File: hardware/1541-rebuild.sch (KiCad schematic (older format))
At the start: 9 parts, among them IC1 ATMEGA1284P-P, SW1 SW_PUSH, SW2 SW_PUSH, SW3 SW_PUSH, X1 20Mhz

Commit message: WPS Signal zum Diskwechsel anzeigen eingebaut. Laden des Track18 eines ausgewählten G64. Schaltpaln aktuallisiert
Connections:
- wire segments 82 -> 85
- no-connect marks 6 -> 5
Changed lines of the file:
@@
 F7 "EN" I B 6950 1900 60
 $EndSheet
-NoConn ~ 6100 4300
 NoConn ~ 6100 4400
 NoConn ~ 6100 4600
@@
 F15 "SOE" I L 6600 4500 60
 F16 "MTR" I R 7700 4300 60
+F17 "WPS" I L 6600 4600 60
 $EndSheet
-Wire Wire Line
-	3400 2900 4100 2900
-Wire Wire Line
-	1800 2900 2000 2900
-Connection ~ 1900 2900
-Wire Wire Line
-	1800 3200 2000 3200
-Connection ~ 1900 3200
-Wire Wire Line
-	4900 5800 4900 5900
-Wire Wire Line
-	4900 5900 5100 5900
-Wire Wire Line
-	5000 5900 5000 5950
-Wire Wire Line
-	5100 5900 5100 5800
-Connection ~ 5000 5900
-Wire Wire Line
-	4900 1800 4900 1700
-Wire Wire Line
-	4900 1700 5100 1700
-Wire Wire Line
-	5000 1700 5000 1650
-Wire Wire Line
-	5100 1700 5100 1800
-Connection ~ 5000 1700
-Wire Wire Line
-	3700 2100 3600 2100
-Wire Wire Line
-	4000 2100 4100 2100
-Wire Wire Line
-	1200 1050 1200 1550
-Connection ~ 1200 1250
-Wire Wire Line
-	1500 1050 1500 1550
-Connection ~ 1500 1250
-Wire Wire Line
-	6450 1900 6450 2100
-Wire Wire Line
-	6450 2100 6100 2100
-Wire Wire Line
-	6550 1900 6550 2200
-Wire Wire Line
-	6550 2200 6100 2200
-Wire Wire Line
-	6650 1900 6650 2300
-Wire Wire Line
-	6650 2300 6100 2300
-Wire Wire Line
-	6750 1900 6750 2400
-Wire Wire Line
-	6750 2400 6100 2400
-Wire Wire Line
-	6850 1900 6850 2500
-Wire Wire Line
-	6850 2500 6100 2500
-Wire Wire Line
-	6950 1900 6950 2600
-Wire Wire Line
-	6950 2600 6100 2600
-Wire Wire Line
-	6100 4800 6600 4800
-Wire Wire Line
-	6100 4900 6600 4900
-Wire Wire Line
-	6100 5000 6600 5000
-Wire Wire Line
-	6100 5100 6600 5100
-Wire Wire Line
-	6100 5200 6600 5200
-Wire Wire Line
-	6100 5300 6600 5300
-Wire Wire Line
-	6100 5400 6600 5400
-Wire Wire Line
-	6100 5500 6600 5500
-Wire Wire Line
-	6100 4500 6600 4500
-Wire Wire Line
-	6100 4000 6300 4000
-Wire Wire Line
-	6300 4000 6300 4400
-Wire Wire Line
-	6300 4400 6600 4400
-Wire Wire Line
-	6100 3900 6400 3900
-Wire Wire Line
-	6400 3900 6400 4300
-Wire Wire Line
-	6400 4300 6600 4300
-Wire Wire Line
-	6100 4100 7850 4100
-Wire Wire Line
-	6100 2700 8150 2700
-Wire Wire Line
-	6100 2800 8050 2800
-Wire Wire Line
-	8150 2700 8150 4500
-Wire Wire Line
-	8050 2800 8050 4400
-Wire Wire Line
-	8050 4400 7700 4400
-Wire Wire Line
-	8150 4500 7700 4500
-Wire Wire Line
-	7850 4100 7850 4300
-Wire Wire Line
-	7850 4300 7700 4300
-Wire Wire Line
-	6100 3400 6800 3400
-Wire Wire Line
-	6100 3500 6800 3500
-Wire Wire Line
-	6100 3600 6800 3600
-Wire Wire Line
-	6100 3700 6800 3700
-Wire Wire Line
-	6100 3300 6550 3300
-Wire Wire Line
-	6550 3300 6550 3150
-Wire Wire Line
-	6550 3150 7850 3150
-Wire Wire Line
-	7850 3150 7850 3400
-Wire Wire Line
-	7850 3400 7750 3400
-Wire Wire Line
-	6100 3200 6450 3200
-Wire Wire Line
-	6450 3200 6450 3050
-Wire Wire Line
-	6450 3050 7950 3050
-Wire Wire Line
-	7950 3050 7950 3500
-Wire Wire Line
-	7950 3500 7750 3500
 $Comp
 L SW_PUSH SW1
@@
 	0    1    1    0
 $EndComp
-Wire Wire Line
-	9100 2850 9200 2850
-Wire Wire Line
-	9200 2850 9200 3450
-Wire Wire Line
-	9100 3150 9300 3150
-Connection ~ 9200 3150
-Wire Wire Line
-	6100 3000 6200 3000
-Wire Wire Line
-	6200 3000 6200 2850
-Wire Wire Line
-	6200 2850 8500 2850
-Wire Wire Line
-	6100 3100 6300 3100
-Wire Wire Line
-	6300 3100 6300 2950
-Wire Wire Line
-	6300 2950 8400 2950
-Wire Wire Line
-	8400 2950 8400 3150
-Wire Wire Line
-	8400 3150 8500 3150
 $Comp
 L SW_PUSH SW3
@@
 $EndComp
 Wire Wire Line
+	3400 2900 4100 2900
+Wire Wire Line
+	1800 2900 2000 2900
+Connection ~ 1900 2900
+Wire Wire Line
+	1800 3200 2000 3200
+Connection ~ 1900 3200
+Wire Wire Line
+	4900 5800 4900 5900
+Wire Wire Line
+	4900 5900 5100 5900
+Wire Wire Line
+	5000 5900 5000 5950
+Wire Wire Line
+	5100 5900 5100 5800
+Connection ~ 5000 5900
+Wire Wire Line
+	4900 1800 4900 1700
+Wire Wire Line
+	4900 1700 5100 1700
+Wire Wire Line
+	5000 1700 5000 1650
+Wire Wire Line
+	5100 1700 5100 1800
+Connection ~ 5000 1700
+Wire Wire Line
+	3700 2100 3600 2100
+Wire Wire Line
+	4000 2100 4100 2100
+Wire Wire Line
+	1200 1050 1200 1550
+Connection ~ 1200 1250
+Wire Wire Line
+	1500 1050 1500 1550
+Connection ~ 1500 1250
+Wire Wire Line
+	6450 1900 6450 2100
+Wire Wire Line
+	6450 2100 6100 2100
+Wire Wire Line
+	6550 1900 6550 2200
+Wire Wire Line
+	6550 2200 6100 2200
+Wire Wire Line
+	6650 1900 6650 2300
+Wire Wire Line
+	6650 2300 6100 2300
+Wire Wire Line
+	6750 1900 6750 2400
+Wire Wire Line
+	6750 2400 6100 2400
+Wire Wire Line
+	6850 1900 6850 2500
+Wire Wire Line
+	6850 2500 6100 2500
+Wire Wire Line
+	6950 1900 6950 2600
+Wire Wire Line
+	6950 2600 6100 2600
+Wire Wire Line
+	6100 4800 6600 4800
+Wire Wire Line
+	6100 4900 6600 4900
+Wire Wire Line
+	6100 5000 6600 5000
+Wire Wire Line
+	6100 5100 6600 5100
+Wire Wire Line
+	6100 5200 6600 5200
+Wire Wire Line
+	6100 5300 6600 5300
+Wire Wire Line
+	6100 5400 6600 5400
+Wire Wire Line
+	6100 5500 6600 5500
+Wire Wire Line
+	6100 4500 6600 4500
+Wire Wire Line
+	6100 4000 6300 4000
+Wire Wire Line
+	6300 4000 6300 4400
+Wire Wire Line
+	6300 4400 6600 4400
+Wire Wire Line
+	6100 3900 6400 3900
+Wire Wire Line
+	6400 3900 6400 4300
+Wire Wire Line
+	6400 4300 6600 4300
+Wire Wire Line
+	6100 4100 7850 4100
+Wire Wire Line
+	6100 2700 8150 2700
+Wire Wire Line
+	6100 2800 8050 2800
+Wire Wire Line
+	8150 2700 8150 4500
+Wire Wire Line
+	8050 2800 8050 4400
+Wire Wire Line
+	8050 4400 7700 4400
+Wire Wire Line
+	8150 4500 7700 4500
+Wire Wire Line
+	7850 4100 7850 4300
+Wire Wire Line
+	7850 4300 7700 4300
+Wire Wire Line
+	6100 3400 6800 3400
+Wire Wire Line
+	6100 3500 6800 3500
+Wire Wire Line
+	6100 3600 6800 3600
+Wire Wire Line
+	6100 3700 6800 3700
+Wire Wire Line
+	6100 3300 6550 3300
+Wire Wire Line
+	6550 3300 6550 3150
+Wire Wire Line
+	6550 3150 7850 3150
+Wire Wire Line
+	7850 3150 7850 3400
+Wire Wire Line
+	7850 3400 7750 3400
+Wire Wire Line
+	6100 3200 6450 3200
+Wire Wire Line
+	6450 3200 6450 3050
+Wire Wire Line
+	6450 3050 7950 3050
+Wire Wire Line
+	7950 3050 7950 3500
+Wire Wire Line
+	7950 3500 7750 3500
+Wire Wire Line
+	9100 2850 9200 2850
+Wire Wire Line
+	9200 2850 9200 3450
+Wire Wire Line
+	9100 3150 9300 3150
+Connection ~ 9200 3150
+Wire Wire Line
+	6100 3000 6200 3000
+Wire Wire Line
+	6200 3000 6200 2850
+Wire Wire Line
+	6200 2850 8500 2850
+Wire Wire Line
+	6100 3100 6300 3100
+Wire Wire Line
+	6300 3100 6300 2950
+Wire Wire Line
+	6300 2950 8400 2950
+Wire Wire Line
+	8400 2950 8400 3150
+Wire Wire Line
+	8400 3150 8500 3150
+Wire Wire Line
 	9200 3450 9100 3450
 Wire Wire Line
@@
 Wire Wire Line
 	8400 3450 8500 3450
+Wire Wire Line
+	6100 4300 6250 4300
+Wire Wire Line
+	6250 4300 6250 4600
+Wire Wire Line
+	6250 4600 6600 4600
 $EndSCHEMATC

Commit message: Im Schaltplan OE an µC PC5 angeschlossen.
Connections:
- wire segments 85 -> 90
- no-connect marks 5 -> 4
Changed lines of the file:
@@
 F7 "EN" I B 6950 1900 60
 $EndSheet
-NoConn ~ 6100 4400
 NoConn ~ 6100 4600
 $Sheet
@@
 Wire Wire Line
 	6250 4600 6600 4600
+Wire Wire Line
+	6200 4400 6200 5700
+Wire Wire Line
+	6200 5700 7850 5700
+Wire Wire Line
+	7850 5700 7850 4600
+Wire Wire Line
+	7850 4600 7700 4600
+Wire Wire Line
+	6200 4400 6100 4400
 $EndSCHEMATC

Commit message: Die 3 Taster müssen auf GND liegen und nich auf +5V ! Es werden die internen PullUps des µC verwendet.
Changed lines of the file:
@@
 EESchema Schematic File Version 2
+LIBS:1541-rebuild-rescue
 LIBS:power
 LIBS:device
@@
 $EndComp
 $Comp
-L +5V #PWR08
-U 1 1 55FEB137
-P 9300 3150
-F 0 "#PWR08" H 9300 3000 50  0001 C CNN
-F 1 "+5V" H 9300 3290 50  0000 C CNN
-F 2 "" H 9300 3150 60  0000 C CNN
-F 3 "" H 9300 3150 60  0000 C CNN
-	1    9300 3150
-	0    1    1    0
-$EndComp
-$Comp
 L SW_PUSH SW3
 U 1 1 55FECA06
@@
 Wire Wire Line
 	6200 4400 6100 4400
+$Comp
+L GND #PWR?
+U 1 1 57D3E94E
+P 9300 3150
+F 0 "#PWR?" H 9300 2900 50  0001 C CNN
+F 1 "GND" H 9300 3000 50  0000 C CNN
+F 2 "" H 9300 3150 60  0000 C CNN
+F 3 "" H 9300 3150 60  0000 C CNN
+	1    9300 3150
+	0    -1   -1   0
+$EndComp
 $EndSCHEMATC

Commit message: diverese Sachen geändert
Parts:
- added P1: ISP, Pin_Headers:Pin_Header_Straight_2x03, symbol CONN_02X03
- C1, C2, C3: footprint Capacitors_ThroughHole:C_Disc_D6_P5 -> Capacitors_THT:C_Disc_D3_P2.5
- SW1, SW2, SW3: footprint (none) -> Buttons_Switches_THT:SW_PUSH-12mm
- X1: footprint Oscillator-Modules:OSCILLATOR_KXO-200_LargePads -> Oscillators:KXO-200_LargePads; symbol TCXO3 -> TCXO3-RESCUE-1541-rebuild
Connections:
- wire segments 90 -> 106
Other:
- moved on the sheet: R1
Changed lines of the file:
@@
 Am meiner 1541II Platine (ASSY NO 345003 REV 9) habe ich folgende modifiktionen durchgeführt:\n- PIN 40 von U10 (Gate Array 251828) von Platine getrennt (BYTE READY)\n- U8 (VIA 6522) ausgelötet und gesockelt\n- Dauerläufer behoben durch trennen einer Leiterbahn (genauer beschreiben)
 $Comp
-L TCXO3 X1
+L TCXO3-RESCUE-1541-rebuild X1
 U 1 1 55F7CB9E
 P 2700 3050
 F 0 "X1" H 2700 3350 70  0000 C CNN
 F 1 "20Mhz" H 2700 3050 70  0000 C CNN
-F 2 "Oscillator-Modules:OSCILLATOR_KXO-200_LargePads" H 2700 3050 60  0001 C CNN
+F 2 "Oscillators:KXO-200_LargePads" H 2700 3050 60  0001 C CNN
 F 3 "" H 2700 3050 60  0000 C CNN
 	1    2700 3050
@@
 F 0 "C3" H 1925 3150 50  0000 L CNN
 F 1 "100n" H 1925 2950 50  0000 L CNN
-F 2 "Capacitors_ThroughHole:C_Disc_D6_P5" H 1938 2900 30  0001 C CNN
+F 2 "Capacitors_THT:C_Disc_D3_P2.5" H 1938 2900 30  0001 C CNN
 F 3 "" H 1900 3050 60  0000 C CNN
 	1    1900 3050
@@
 L R R1
 U 1 1 55F7EA97
-P 3850 2100
-F 0 "R1" V 3930 2100 50  0000 C CNN
-F 1 "10k" V 3850 2100 50  0000 C CNN
-F 2 "Resistors_ThroughHole:Resistor_Horizontal_RM10mm" V 3780 2100 30  0001 C CNN
-F 3 "" H 3850 2100 30  0000 C CNN
-	1    3850 2100
+P 3800 2100
+F 0 "R1" V 3880 2100 50  0000 C CNN
+F 1 "10k" V 3800 2100 50  0000 C CNN
+F 2 "Resistors_ThroughHole:Resistor_Horizontal_RM10mm" V 3730 2100 30  0001 C CNN
+F 3 "" H 3800 2100 30  0000 C CNN
+	1    3800 2100
 	0    1    1    0
 $EndComp
@@
 L +5V #PWR05
 U 1 1 55F7ED10
-P 3600 2100
-F 0 "#PWR05" H 3600 1950 50  0001 C CNN
-F 1 "+5V" H 3600 2240 50  0000 C CNN
-F 2 "" H 3600 2100 60  0000 C CNN
-F 3 "" H 3600 2100 60  0000 C CNN
-	1    3600 2100
+P 3500 2100
+F 0 "#PWR05" H 3500 1950 50  0001 C CNN
+F 1 "+5V" H 3500 2240 50  0000 C CNN
+F 2 "" H 3500 2100 60  0000 C CNN
+F 3 "" H 3500 2100 60  0000 C CNN
+	1    3500 2100
 	0    -1   -1   0
 $EndComp
@@
 F 0 "C1" H 1375 1350 50  0000 L CNN
 F 1 "100n" H 1375 1150 50  0000 L CNN
-F 2 "Capacitors_ThroughHole:C_Disc_D6_P5" H 1388 1100 30  0001 C CNN
+F 2 "Capacitors_THT:C_Disc_D3_P2.5" H 1388 1100 30  0001 C CNN
 F 3 "" H 1350 1250 60  0000 C CNN
 	1    1350 1250
@@
 F 0 "C2" H 1375 1650 50  0000 L CNN
 F 1 "100n" H 1375 1450 50  0000 L CNN
-F 2 "Capacitors_ThroughHole:C_Disc_D6_P5" H 1388 1400 30  0001 C CNN
+F 2 "Capacitors_THT:C_Disc_D3_P2.5" H 1388 1400 30  0001 C CNN
 F 3 "" H 1350 1550 60  0000 C CNN
 	1    1350 1550
@@
 Stützkondensatoren für IC1
 $Sheet
-S 6800 3300 950  450
+S 7550 3300 950  450
 U 55F7A0F9
 F0 "SD Karte" 60
 F1 "sd_karte.sch" 60
-F2 "MISO" I L 6800 3600 60
-F3 "SCK" I L 6800 3700 60
-F4 "MOSI" I L 6800 3500 60
-F5 "SS" I L 6800 3400 60
-F6 "SD_DETECT" I R 7750 3500 60
-F7 "SD_WP" I R 7750 3400 60
+F2 "MISO" I L 7550 3600 60
+F3 "SCK" I L 7550 3700 60
+F4 "MOSI" I L 7550 3500 60
+F5 "SS" I L 7550 3400 60
+F6 "SD_DETECT" I R 8500 3500 60
+F7 "SD_WP" I R 8500 3400 60
 $EndSheet
 $Sheet
@@
 L SW_PUSH SW1
 U 1 1 55FEAE1B
-P 8800 2850
-F 0 "SW1" H 8950 2960 50  0000 C CNN
-F 1 "SW_PUSH" H 8800 2770 50  0000 C CNN
-F 2 "" H 8800 2850 60  0000 C CNN
-F 3 "" H 8800 2850 60  0000 C CNN
-	1    8800 2850
+P 9450 2850
+F 0 "SW1" H 9600 2960 50  0000 C CNN
+F 1 "SW_PUSH" H 9450 2770 50  0000 C CNN
+F 2 "Buttons_Switches_THT:SW_PUSH-12mm" H 9450 2850 60  0001 C CNN
+F 3 "" H 9450 2850 60  0000 C CNN
+	1    9450 2850
 	1    0    0    -1
 $EndComp
@@
 L SW_PUSH SW2
 U 1 1 55FEAF42
-P 8800 3150
-F 0 "SW2" H 8950 3260 50  0000 C CNN
-F 1 "SW_PUSH" H 8800 3070 50  0000 C CNN
-F 2 "" H 8800 3150 60  0000 C CNN
-F 3 "" H 8800 3150 60  0000 C CNN
-	1    8800 3150
+P 9450 3150
+F 0 "SW2" H 9600 3260 50  0000 C CNN
+F 1 "SW_PUSH" H 9450 3070 50  0000 C CNN
+F 2 "Buttons_Switches_THT:SW_PUSH-12mm" H 9450 3150 60  0001 C CNN
+F 3 "" H 9450 3150 60  0000 C CNN
+	1    9450 3150
 	1    0    0    -1
 $EndComp
@@
 L SW_PUSH SW3
 U 1 1 55FECA06
-P 8800 3450
-F 0 "SW3" H 8950 3560 50  0000 C CNN
-F 1 "SW_PUSH" H 8800 3370 50  0000 C CNN
-F 2 "" H 8800 3450 60  0000 C CNN
-F 3 "" H 8800 3450 60  0000 C CNN
-	1    8800 3450
+P 9450 3450
+F 0 "SW3" H 9600 3560 50  0000 C CNN
+F 1 "SW_PUSH" H 9450 3370 50  0000 C CNN
+F 2 "Buttons_Switches_THT:SW_PUSH-12mm" H 9450 3450 60  0001 C CNN
+F 3 "" H 9450 3450 60  0000 C CNN
+	1    9450 3450
 	1    0    0    -1
 $EndComp
@@
 Connection ~ 5000 1700
 Wire Wire Line
-	3700 2100 3600 2100
-Wire Wire Line
-	4000 2100 4100 2100
+	3650 2100 3500 2100
+Wire Wire Line
+	3950 2100 4100 2100
 Wire Wire Line
 	1200 1050 1200 1550
@@
 	6100 4100 7850 4100
 Wire Wire Line
-	6100 2700 8150 2700
-Wire Wire Line
-	6100 2800 8050 2800
-Wire Wire Line
-	8150 2700 8150 4500
-Wire Wire Line
-	8050 2800 8050 4400
-Wire Wire Line
-	8050 4400 7700 4400
-Wire Wire Line
-	8150 4500 7700 4500
+	6100 2700 8950 2700
+Wire Wire Line
+	6100 2800 8850 2800
+Wire Wire Line
+	8950 2700 8950 4500
+Wire Wire Line
+	8850 2800 8850 4400
+Wire Wire Line
+	8850 4400 7700 4400
+Wire Wire Line
+	8950 4500 7700 4500
 Wire Wire Line
 	7850 4100 7850 4300
@@
 	7850 4300 7700 4300
 Wire Wire Line
-	6100 3400 6800 3400
-Wire Wire Line
-	6100 3500 6800 3500
-Wire Wire Line
-	6100 3600 6800 3600
-Wire Wire Line
-	6100 3700 6800 3700
+	6100 3400 7550 3400
+Wire Wire Line
+	6100 3500 7550 3500
+Wire Wire Line
+	6100 3600 7550 3600
+Wire Wire Line
+	6100 3700 7550 3700
 Wire Wire Line
 	6100 3300 6550 3300
@@
 	6550 3300 6550 3150
 Wire Wire Line
-	6550 3150 7850 3150
-Wire Wire Line
-	7850 3150 7850 3400
-Wire Wire Line
-	7850 3400 7750 3400
+	6550 3150 8650 3150
+Wire Wire Line
+	8650 3150 8650 3400
+Wire Wire Line
+	8650 3400 8500 3400
 Wire Wire Line
 	6100 3200 6450 3200
@@
 	6450 3200 6450 3050
 Wire Wire Line
-	6450 3050 7950 3050
-Wire Wire Line
-	7950 3050 7950 3500
-Wire Wire Line
-	7950 3500 7750 3500
-Wire Wire Line
-	9100 2850 9200 2850
-Wire Wire Line
-	9200 2850 9200 3450
-Wire Wire Line
-	9100 3150 9300 3150
-Connection ~ 9200 3150
+	6450 3050 8750 3050
+Wire Wire Line
+	8750 3050 8750 3500
+Wire Wire Line
+	8750 3500 8500 3500
+Wire Wire Line
+	9750 2850 9850 2850
+Wire Wire Line
+	9850 2850 9850 3450
+Wire Wire Line
+	9750 3150 9950 3150
+Connection ~ 9850 3150
 Wire Wire Line
 	6100 3000 6200 3000
@@
 	6200 3000 6200 2850
 Wire Wire Line
-	6200 2850 8500 2850
+	6200 2850 9150 2850
 Wire Wire Line
 	6100 3100 6300 3100
@@
 	6300 3100 6300 2950
 Wire Wire Line
-	6300 2950 8400 2950
-Wire Wire Line
-	8400 2950 8400 3150
-Wire Wire Line
-	8400 3150 8500 3150
-Wire Wire Line
-	9200 3450 9100 3450
+	6300 2950 9050 2950
+Wire Wire Line
+	9050 2950 9050 3150
+Wire Wire Line
+	9050 3150 9150 3150
+Wire Wire Line
+	9850 3450 9750 3450
 Wire Wire Line
 	6100 4200 6500 4200
@@
 	6500 4200 6500 3900
 Wire Wire Line
-	6500 3900 8400 3900
-Wire Wire Line
-	8400 3900 8400 3450
-Wire Wire Line
-	8400 3450 8500 3450
+	6500 3900 9050 3900
+Wire Wire Line
+	9050 3900 9050 3450
+Wire Wire Line
+	9050 3450 9150 3450
 Wire Wire Line
 	6100 4300 6250 4300
@@
 	6200 4400 6100 4400
 $Comp
-L GND #PWR?
+L GND #PWR08
 U 1 1 57D3E94E
-P 9300 3150
-F 0 "#PWR?" H 9300 2900 50  0001 C CNN
-F 1 "GND" H 9300 3000 50  0000 C CNN
-F 2 "" H 9300 3150 60  0000 C CNN
-F 3 "" H 9300 3150 60  0000 C CNN
-	1    9300 3150
+P 9950 3150
+F 0 "#PWR08" H 9950 2900 50  0001 C CNN
+F 1 "GND" H 9950 3000 50  0000 C CNN
+F 2 "" H 9950 3150 60  0000 C CNN
+F 3 "" H 9950 3150 60  0000 C CNN
+	1    9950 3150
 	0    -1   -1   0
 $EndComp
+$Comp
+L CONN_02X03 P1
+U 1 1 5840690C
+P 7850 1600
+F 0 "P1" H 7850 1915 50  0000 C CNN
+F 1 "ISP" H 7850 1824 50  0000 C CNN
+F 2 "Pin_Headers:Pin_Header_Straight_2x03" H 7850 400 50  0001 C CNN
+F 3 "" H 7850 400 50  0000 C CNN
+	1    7850 1600
+	1    0    0    -1
+$EndComp
+Wire Wire Line
+	7600 1500 7150 1500
+Wire Wire Line
+	7150 1500 7150 3600
+Connection ~ 7150 3600
+Wire Wire Line
+	7600 1600 7200 1600
+Wire Wire Line
+	7200 1600 7200 3700
+Connection ~ 7200 3700
+Wire Wire Line
+	4050 2100 4050 1000
+Wire Wire Line
+	4050 1000 7400 1000
+Wire Wire Line
+	7400 1000 7400 1700
+Wire Wire Line
+	7400 1700 7600 1700
+Connection ~ 4050 2100
+$Comp
+L +5V #PWR09
+U 1 1 58409984
+P 8300 1450
+F 0 "#PWR09" H 8300 1300 50  0001 C CNN
+F 1 "+5V" H 8300 1590 50  0000 C CNN
+F 2 "" H 8300 1450 60  0000 C CNN
+F 3 "" H 8300 1450 60  0000 C CNN
+	1    8300 1450
+	1    0    0    -1
+$EndComp
+Wire Wire Line
+	8100 1500 8300 1500
+Wire Wire Line
+	8300 1500 8300 1450
+$Comp
+L GND #PWR010
+U 1 1 58409C3B
+P 8300 1750
+F 0 "#PWR010" H 8300 1500 50  0001 C CNN
+F 1 "GND" H 8300 1600 50  0000 C CNN
+F 2 "" H 8300 1750 60  0000 C CNN
+F 3 "" H 8300 1750 60  0000 C CNN
+	1    8300 1750
+	1    0    0    -1
+$EndComp
+Wire Wire Line
+	8100 1700 8300 1700
+Wire Wire Line
+	8300 1700 8300 1750
+Wire Wire Line
+	8100 1600 8400 1600
+Wire Wire Line
+	8400 1600 8400 2250
+Wire Wire Line
+	8400 2250 7250 2250
+Wire Wire Line
+	7250 2250 7250 3500
+Connection ~ 7250 3500
 $EndSCHEMATC

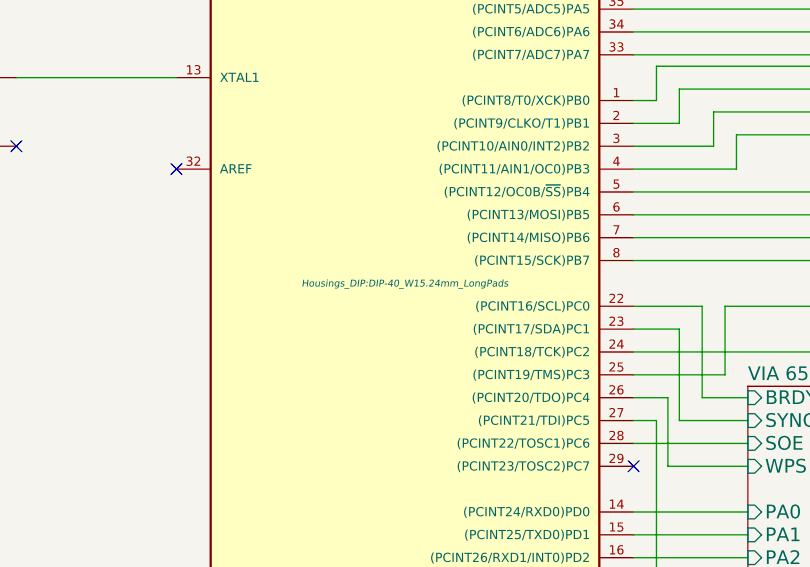
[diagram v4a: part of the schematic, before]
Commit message: Platine per Autorouter geroutet.
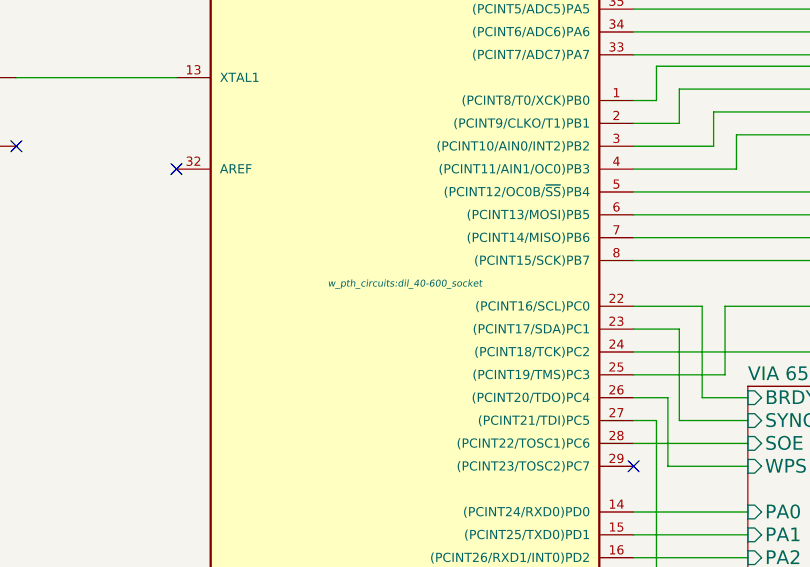
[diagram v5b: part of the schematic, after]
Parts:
- C1, C2, C3: footprint Capacitors_THT:C_Disc_D3_P2.5 -> w_capacitors:cnp_3mm_disc
- IC1: footprint Housings_DIP:DIP-40_W15.24mm_LongPads -> w_pth_circuits:dil_40-600_socket
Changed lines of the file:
@@
 LIBS:valves
 LIBS:Oscillators
+LIBS:w_analog
+LIBS:w_connectors
+LIBS:w_device
+LIBS:w_logic
+LIBS:w_memory
+LIBS:w_microcontrollers
+LIBS:w_opto
+LIBS:w_relay
+LIBS:w_rtx
+LIBS:w_transistor
+LIBS:w_vacuum
 LIBS:1541-rebuild-cache
 EELAYER 25 0
@@
 F 0 "IC1" H 4250 5680 40  0000 L BNN
 F 1 "ATMEGA1284P-P" H 5500 1850 40  0000 L BNN
-F 2 "Housings_DIP:DIP-40_W15.24mm_LongPads" H 5100 3800 30  0000 C CIN
+F 2 "w_pth_circuits:dil_40-600_socket" H 5100 3800 30  0000 C CIN
 F 3 "" H 5100 3800 60  0000 C CNN
 	1    5100 3800
@@
 F 0 "C3" H 1925 3150 50  0000 L CNN
 F 1 "100n" H 1925 2950 50  0000 L CNN
-F 2 "Capacitors_THT:C_Disc_D3_P2.5" H 1938 2900 30  0001 C CNN
+F 2 "w_capacitors:cnp_3mm_disc" H 1938 2900 30  0001 C CNN
 F 3 "" H 1900 3050 60  0000 C CNN
 	1    1900 3050
@@
 F 0 "C1" H 1375 1350 50  0000 L CNN
 F 1 "100n" H 1375 1150 50  0000 L CNN
-F 2 "Capacitors_THT:C_Disc_D3_P2.5" H 1388 1100 30  0001 C CNN
+F 2 "w_capacitors:cnp_3mm_disc" H 1388 1100 30  0001 C CNN
 F 3 "" H 1350 1250 60  0000 C CNN
 	1    1350 1250
@@
 F 0 "C2" H 1375 1650 50  0000 L CNN
 F 1 "100n" H 1375 1450 50  0000 L CNN
-F 2 "Capacitors_THT:C_Disc_D3_P2.5" H 1388 1400 30  0001 C CNN
+F 2 "w_capacitors:cnp_3mm_disc" H 1388 1400 30  0001 C CNN
 F 3 "" H 1350 1550 60  0000 C CNN
 	1    1350 1550

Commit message: PCB Board gelöscht um mit älteren KiCad Versionen kompatibel zu sein.
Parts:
- SW1, SW2, SW3: symbol SW_PUSH -> SW_PUSH-RESCUE-1541-rebuild
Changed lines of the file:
@@
 $EndSheet
 $Comp
-L SW_PUSH SW1
+L SW_PUSH-RESCUE-1541-rebuild SW1
 U 1 1 55FEAE1B
 P 9450 2850
@@
 $EndComp
 $Comp
-L SW_PUSH SW2
+L SW_PUSH-RESCUE-1541-rebuild SW2
 U 1 1 55FEAF42
 P 9450 3150
@@
 $EndComp
 $Comp
-L SW_PUSH SW3
+L SW_PUSH-RESCUE-1541-rebuild SW3
 U 1 1 55FECA06
 P 9450 3450
